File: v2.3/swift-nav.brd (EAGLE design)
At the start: 53 x 53 mm, 150 parts, among them J1 SMA_EDGE, J6 ZX62-B-5PA, Q1 IRLML6401, U1 6SLX9FTG256, U10 MAX2769, U12 PT7M8206B33TA5EX, U13 M25PX80, U2 LTC3407A_DFN, U3 STM32-M-64-LQFP, U4 7Q-16.368MBG-T, U5 SMA_PATCH_SMDGND, U6 93LC56BT-I/OT, U7 FT232HQ, U8 B4050, U9 XC2401, X3 FPGA DEBUG, X4 NX5032GA-12M, X5 CONN_5-2

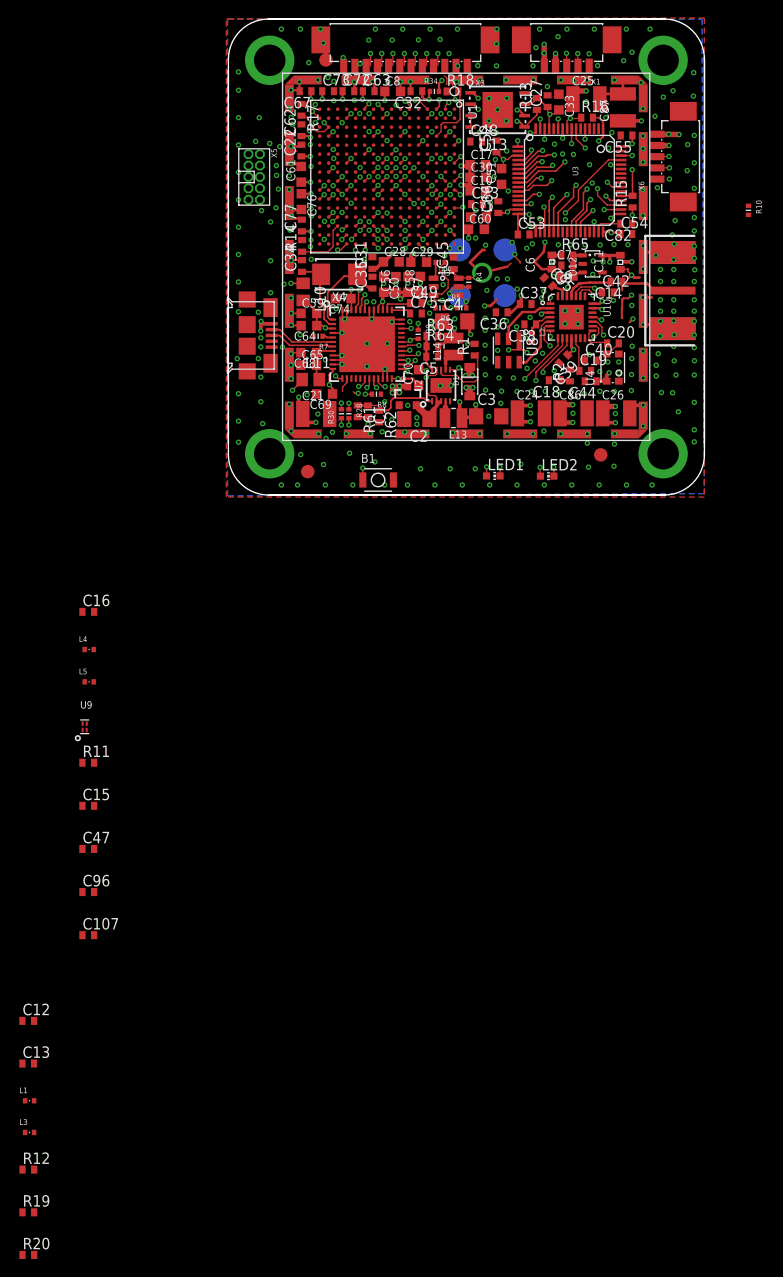
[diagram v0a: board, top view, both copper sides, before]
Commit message: Changed cap footprints to smaller versions
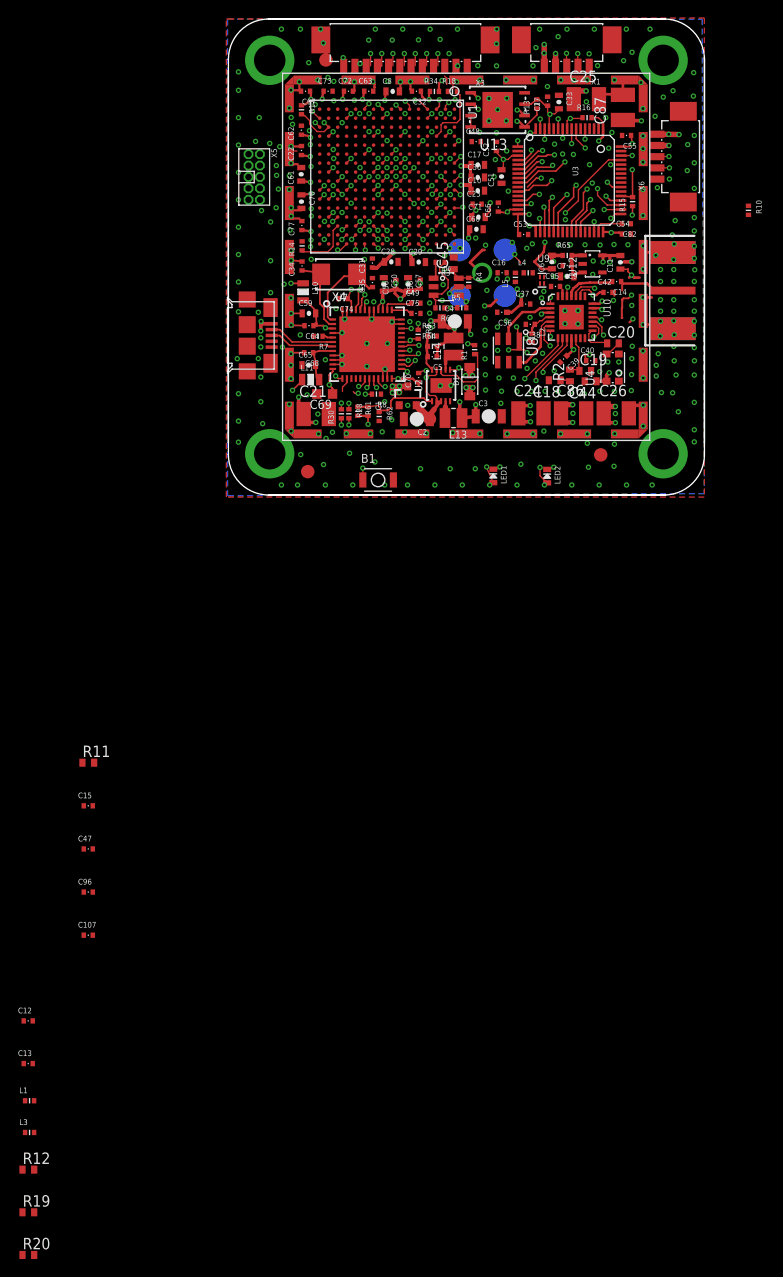
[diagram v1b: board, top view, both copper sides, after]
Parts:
- C1, C107, C12, C13, C14, C15, C16, C22, C23, C27, C31, C32, C34, C35, C36, C37, C38, C39, C40, C42, C47, C48, C49, C5, C52, C53, C54, C55, C62, C63, C66, C67, C72, C73, C75, C77, C82, C9, C95, C96: device rcl:C0402 -> pel_dipol_comp:0402-CAP
- C10, C17, C28, C29, C30, C33, C50, C51, C57, C59, C60, C61, C65, C71, C76, C8: device rcl:C0603K -> pel_dipol_comp:0603-CAP
- C11, C6, C7: device capsmd:0603 -> pel_dipol_comp:0603-CAP
- C2, C3, C4: device rcl:C1206 -> pel_dipol_comp:1206-CAP
- C21, C24, C25, C26, C86, C87: device rcl:C1210K -> rcl:C1210
- C56, C58, C64, C68, C70, C74: device rcl:C0603K -> pel_dipol_comp:0402-CAP
- L10, L11: device rcl:R0805 -> pel_dipol_comp:0805-IND
- L4: value 3.3nH -> 5.1nH
- L5: value 5.1nH -> 3.3nH
- LED1, LED2: device led:CHIP-LED0603 -> pel_dipol_comp:0603-LED
- R1, R13, R14, R15, R16, R17, R18, R61, R62, R63, R64, R65: device rcl:R0402 -> pel_dipol_comp:0402-RES
- moved U9 71.2 mm to (38.3, 27.3)
- moved L5 65.4 mm to (35.4, 27.6), turned to 90 degrees
- moved L4 64.4 mm to (36.8, 28.1)
- moved C16 59.6 mm to (33.9, 28.1)
- moved C95 0.95 mm to (39.8, 26.6), turned to 0 degrees
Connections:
- new net N$1: X3.12
- net FPGA_DONE: now also R16.P$1; no longer R16.1
- net FPGA_INIT_B: now also R17.P$2; no longer R17.2
- net FPGA_PROGRAM_B: now also R15.P$2; no longer R15.2
- net GND: now also C10.P$2, C107.P$2, C11.P$1, C12.P$1, C13.P$1, C15.P$1, C17.P$2, C2.P$2, C22.P$2, C23.P$2, C27.P$2, C28.P$2, C29.P$2, C3.P$2, C30.P$2, C31.P$2, C32.P$2, C33.P$1, C34.P$2, C35.P$2, C36.P$2, C37.P$2, C38.P$2, C39.P$2, C4.P$2, C40.P$2, C42.P$2, C47.P$1, C48.P$2, C49.P$2, C50.P$1, C51.P$1, C52.P$2, C53.P$2, C54.P$2, C55.P$2, C56.P$2, C57.P$1, C58.P$2, C59.P$1, C6.P$1, C60.P$2, C61.P$2, C62.P$2, C63.P$2, C64.P$2, C65.P$1, C66.P$2, C67.P$2, C68.P$2, C7.P$1, C70.P$2, C71.P$2, C72.P$2, C73.P$2, C74.P$2, C75.P$2, C76.P$2, C77.P$2, C8.P$2, C82.P$1, C9.P$2, C96.P$2, L5.P$1, R14.P$2, R18.P$1, R62.P$2, R63.P$2; no longer C10.2, C107.2, C11.1, C12.1, C13.1, C15.1, C17.2, C2.2, C22.2, C23.2, C27.2, C28.2, C29.2, C3.2, C30.2, C31.2, C32.2, C33.1, C34.2, C35.2, C36.2, C37.2, C38.2, C39.2, C4.2, C40.2, C42.2, C47.1, C48.2, C49.2, C50.1, C51.1, C52.2, C53.2, C54.2, C55.2, C56.2, C57.1, C58.2, C59.1, C6.1, C60.2, C61.2, C62.2, C63.2, C64.2, C65.1, C66.2, C67.2, C68.2, C7.1, C70.2, C71.2, C72.2, C73.2, C74.2, C75.2, C76.2, C77.2, C8.2, C82.1, C9.2, C96.2, L4.P$1, R14.2, R18.1, R62.2, R63.2
- net JTAG_RST: now also C32.P$1; no longer C32.1
- net N$11: now also C95.P$2; no longer C95.2
- net N$14: now also C16.P$1; no longer C16.1
- net N$15: now also C35.P$1; no longer C35.1
- net N$16: now also R1.P$1; no longer R1.1
- net N$19: now also C49.P$1; no longer C49.1
- net N$2: now also L4.P$2; no longer L5.P$1
- net N$21: now also C65.P$2, C68.P$1, L11.P$2; no longer C65.2, C68.1, L11.2
- net N$22: now also C38.P$1; no longer C38.1
- net N$29: now also C59.P$2, C64.P$1, L10.P$2; no longer C59.2, C64.1, L10.2
- net N$30: now also C14.P$2; no longer C14.2
- net N$31: now also R18.P$2; no longer R18.2
- net N$32: now also C75.P$1; no longer C75.1
- net N$34: now also R14.P$1; no longer R14.1
- net N$35: now also C16.P$2, L4.P$1; no longer C16.2, L4.P$2
- net N$36: now also C95.P$1; no longer C95.1
- net N$37: now also C12.P$2, C13.P$2; no longer C12.2, C13.2
- net N$41: now also C15.P$2, C47.P$2; no longer C15.2, C47.2
- net N$53: now also C1.P$1, R61.P$1, R62.P$1; no longer C1.1, R61.1, R62.1
- net N$54: now also C5.P$2, R63.P$1, R64.P$1; no longer C5.2, R63.1, R64.1
- net N$56: now also C7.P$2, C9.P$1, R65.P$2; no longer C7.2, C9.1, R65.2
- net N$8: now also C14.P$1; no longer C14.1
- net N$9: now also C34.P$1; no longer C34.1
- net SPI2NSS_FLASH: now also R13.P$1; no longer R13.1
- net V+: no longer X3.12
- net VCC: now also C11.P$2, C36.P$1, C37.P$1, C39.P$1, C40.P$1, C42.P$1; no longer C11.2, C36.1, C37.1, C39.1, C40.1, C42.1
- net VCCINT: now also C10.P$1, C17.P$1, C28.P$1, C29.P$1, C30.P$1, C31.P$1, C4.P$1, C5.P$1, R64.P$2; no longer C10.1, C17.1, C28.1, C29.1, C30.1, C31.1, C4.1, C5.1, R64.2
- net VCCIO: now also C1.P$2, C107.P$1, C22.P$1, C23.P$1, C27.P$1, C3.P$1, C33.P$2, C48.P$1, C50.P$2, C51.P$2, C52.P$1, C53.P$1, C54.P$1, C55.P$1, C56.P$1, C57.P$2, C58.P$1, C60.P$1, C61.P$1, C62.P$1, C63.P$1, C67.P$1, C70.P$1, C71.P$1, C72.P$1, C73.P$1, C74.P$1, C76.P$1, C77.P$1, C8.P$1, C96.P$1, L10.P$1, L11.P$1, R13.P$2, R15.P$1, R16.P$2, R17.P$1, R61.P$2; no longer C1.2, C107.1, C22.1, C23.1, C27.1, C3.1, C33.2, C48.1, C50.2, C51.2, C52.1, C53.1, C54.1, C55.1, C56.1, C57.2, C58.1, C60.1, C61.1, C62.1, C63.1, C67.1, C70.1, C71.1, C72.1, C73.1, C74.1, C76.1, C77.1, C8.1, C96.1, L10.1, L11.1, R13.2, R15.1, R16.2, R17.1, R61.2
- net VDD: now also C2.P$1, C6.P$2, R1.P$2, R65.P$1; no longer C2.1, C6.2, R1.2, R65.1
- net VSS1: now also C66.P$1; no longer C66.1
- net VSS2: now also C82.P$2; no longer C82.2
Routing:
- net N$14: track 3.46 -> 0.00 mm
- net VCCIO: track 143.7 -> 146.7 mm
- net GND: track 80.4 -> 81.9 mm
- net N$11: track 1.89 -> 0.70 mm
- net N$55: track 25.5 -> 26.5 mm
- net N$24: track 20.6 -> 21.5 mm
- net VCC: track 14.3 -> 15.0 mm
- net N$29: track 5.97 -> 6.50 mm
- net VCCINT: track 76.1 -> 76.7 mm

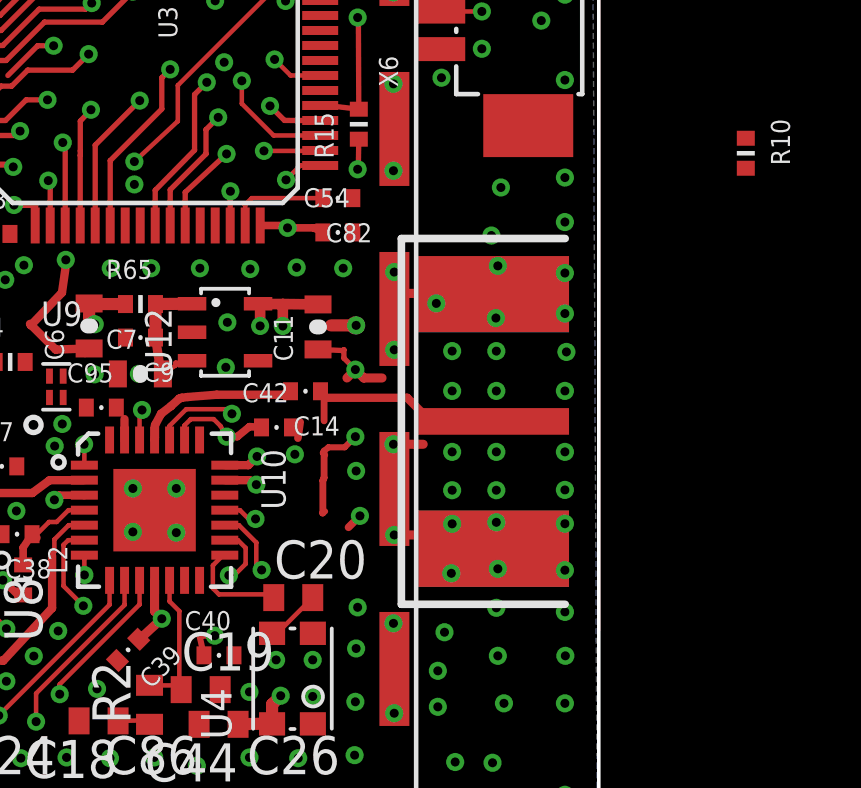
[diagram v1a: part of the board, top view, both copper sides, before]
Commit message: Moved LNA2 SMA to line up with shield opening better
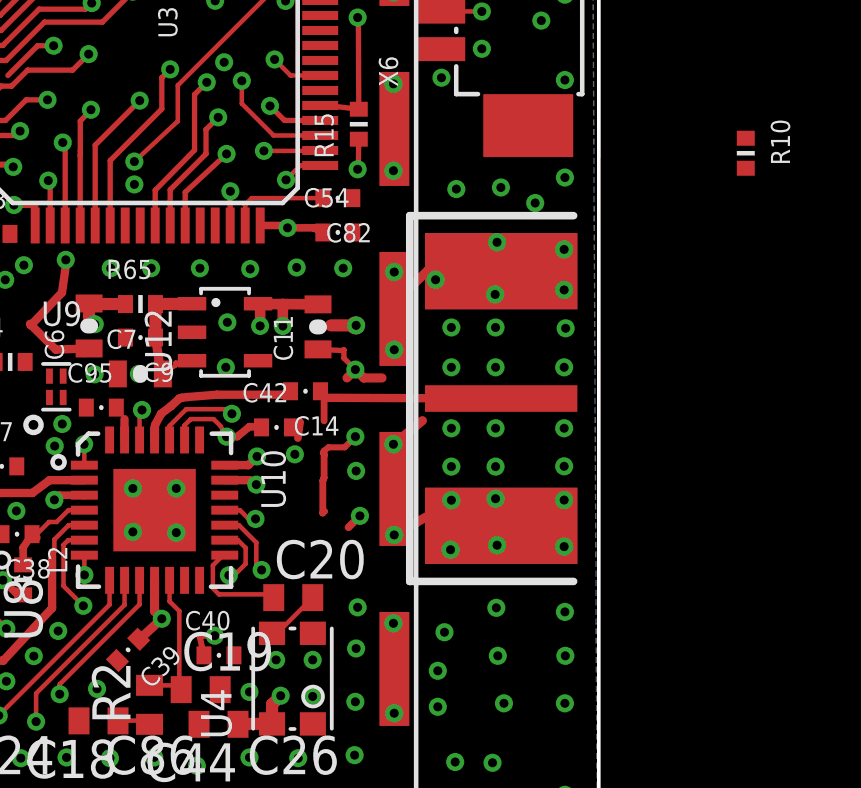
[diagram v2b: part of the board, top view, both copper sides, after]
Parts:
- moved J1 0.81 mm to (55.7, 26.9)
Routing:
- net GND: track 81.9 -> 82.6 mm
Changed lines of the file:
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@@
 <layer number="49" name="Reference" color="7" fill="1" visible="no" active="yes"/>
 <layer number="50" name="dxf" color="7" fill="1" visible="no" active="no"/>
-<layer number="51" name="tDocu" color="7" fill="1" visible="yes" active="yes"/>
+<layer number="51" name="tDocu" color="7" fill="1" visible="no" active="yes"/>
 <layer number="52" name="bDocu" color="7" fill="1" visible="no" active="yes"/>
 <layer number="53" name="tGND_GNDA" color="7" fill="9" visible="no" active="no"/>
@@
 <element name="B1" library="jobygnss" package="B3U-1000P" value="B3U-1000P" x="20.066" y="5.08"/>
 <element name="U5" library="joby_robotics" package="SMA_PATCH_SMDGND" value="SMA_PATCH_SMDGND" x="29.9" y="29.9" rot="MR270"/>
-<element name="J1" library="swift-nav" package="SMA_EDGE" value="SMA_EDGE" x="55.407559375" y="26.162" smashed="yes" rot="R270"/>
+<element name="J1" library="swift-nav" package="SMA_EDGE" value="SMA_EDGE" x="55.686959375" y="26.924" smashed="yes" rot="R270"/>
 <element name="C2" library="pel_dipol_comp" package="1206-CAP" value="10uF" x="24.3796" y="11.8646" rot="R180"/>
 <element name="C3" library="pel_dipol_comp" package="1206-CAP" value="10uF" x="32.385" y="12.1666"/>
@@
 <via x="55.2704" y="16.764" extent="1-16" drill="0.3"/>
 <via x="55.2704" y="19.812" extent="1-16" drill="0.3"/>
-<via x="55.2704" y="22.752" extent="1-16" drill="0.3"/>
-<via x="55.2704" y="25.146" extent="1-16" drill="0.3"/>
-<via x="55.2704" y="27.178" extent="1-16" drill="0.3"/>
-<via x="55.2704" y="31.107" extent="1-16" drill="0.3"/>
+<via x="55.245" y="23.5394" extent="1-16" drill="0.3"/>
+<via x="55.245" y="25.9334" extent="1-16" drill="0.3"/>
+<via x="55.245" y="27.9654" extent="1-16" drill="0.3"/>
+<via x="55.245" y="31.8944" extent="1-16" drill="0.3"/>
 <via x="55.2704" y="34.29" extent="1-16" drill="0.3"/>
 <via x="55.2704" y="37.5412" extent="1-16" drill="0.3"/>
@@
 <via x="25.4254" y="10.2616" extent="1-16" drill="0.3"/>
 <via x="10.1854" y="13.5128" extent="1-16" drill="0.3"/>
-<via x="52.9844" y="27.178" extent="1-16" drill="0.3"/>
-<via x="52.9844" y="25.146" extent="1-16" drill="0.3"/>
+<via x="52.959" y="27.9654" extent="1-16" drill="0.3"/>
+<via x="52.959" y="25.9334" extent="1-16" drill="0.3"/>
 <wire x1="31.9278" y1="30.6832" x2="31.6738" y2="30.6832" width="0.3048" layer="1"/>
 <wire x1="31.6738" y1="30.6832" x2="30.3022" y2="29.3116" width="0.3048" layer="1"/>
@@
 <wire x1="31.9278" y1="24.4602" x2="32.5882" y2="24.4602" width="0.3048" layer="1"/>
 <wire x1="32.5882" y1="24.4602" x2="33.274" y2="25.146" width="0.3048" layer="1"/>
-<wire x1="49.5808" y1="22.3774" x2="51.0032" y2="22.3774" width="0.3048" layer="1"/>
-<wire x1="51.0032" y1="22.3774" x2="51.054" y2="22.3266" width="0.3048" layer="1"/>
+<wire x1="49.5808" y1="22.3774" x2="50.9778" y2="23.1648" width="0.3048" layer="1"/>
+<wire x1="50.9778" y1="23.1648" x2="51.0286" y2="23.114" width="0.3048" layer="1"/>
 <wire x1="49.586" y1="29.91" x2="49.586" y2="30.1042" width="0.3048" layer="1"/>
 <wire x1="49.586" y1="30.1042" x2="49.911" y2="30.4292" width="0.3048" layer="1"/>
-<wire x1="49.911" y1="30.4292" x2="50.7492" y2="30.4292" width="0.3048" layer="1"/>
-<wire x1="50.7492" y1="30.4292" x2="50.7746" y2="30.4038" width="0.3048" layer="1"/>
-<via x="51.5112" y="27.178" extent="1-16" drill="0.3"/>
-<via x="51.5112" y="25.146" extent="1-16" drill="0.3"/>
+<wire x1="49.911" y1="30.4292" x2="50.7238" y2="31.2166" width="0.3048" layer="1"/>
+<wire x1="50.7238" y1="31.2166" x2="50.7492" y2="31.1912" width="0.3048" layer="1"/>
+<via x="51.4858" y="27.9654" extent="1-16" drill="0.3"/>
+<via x="51.4858" y="25.9334" extent="1-16" drill="0.3"/>
 <via x="8.1026" y="29.4894" extent="1-16" drill="0.3"/>
 <via x="8.1026" y="25.9334" extent="1-16" drill="0.3"/>
@@
 <via x="53.2384" y="16.764" extent="1-16" drill="0.3"/>
 <via x="51.2564" y="19.134" extent="1-16" drill="0.3"/>
-<via x="52.9844" y="22.798" extent="1-16" drill="0.3"/>
-<via x="51.5112" y="22.748" extent="1-16" drill="0.3"/>
-<via x="53.0344" y="31.346" extent="1-16" drill="0.3"/>
+<via x="52.959" y="23.5854" extent="1-16" drill="0.3"/>
+<via x="51.4858" y="23.5354" extent="1-16" drill="0.3"/>
+<via x="53.009" y="32.1334" extent="1-16" drill="0.3"/>
 <via x="49.5554" y="41.9608" extent="1-16" drill="0.3"/>
 <via x="6.8326" y="45.4152" extent="1-16" drill="0.3"/>
@@
 <wire x1="48.4378" y1="23.0124" x2="48.0568" y2="22.6314" width="0.254" layer="1"/>
 <wire x1="46.370240625" y1="25.60263125" x2="46.446440625" y2="26.13968125" width="0.254" layer="1"/>
-<wire x1="49.5554" y1="25.4" x2="50.546" y2="25.4" width="0.3048" layer="1"/>
+<wire x1="49.5554" y1="25.4" x2="50.5206" y2="26.1874" width="0.3048" layer="1"/>
 <wire x1="48.2854" y1="27.8892" x2="48.3362" y2="27.8384" width="0.3048" layer="1"/>
 <wire x1="48.3362" y1="27.8384" x2="48.5648" y2="27.6098" width="0.3048" layer="1"/>
@@
 <via x="8.7122" y="35.3822" extent="1-16" drill="0.3"/>
 <via x="6.4262" y="42.7736" extent="1-16" drill="0.3"/>
-<via x="52.9844" y="28.506" extent="1-16" drill="0.3"/>
-<via x="51.5112" y="28.506" extent="1-16" drill="0.3"/>
-<via x="52.9844" y="23.868" extent="1-16" drill="0.3"/>
-<via x="51.5112" y="23.868" extent="1-16" drill="0.3"/>
+<via x="52.959" y="29.2934" extent="1-16" drill="0.3"/>
+<via x="51.4858" y="29.2934" extent="1-16" drill="0.3"/>
+<via x="52.959" y="24.6554" extent="1-16" drill="0.3"/>
+<via x="51.4858" y="24.6554" extent="1-16" drill="0.3"/>
 <contactref element="H2" pad="B3,0"/>
 <contactref element="H4" pad="B3,0"/>
@@
 <via x="41.81034375" y="41.31880625" extent="1-16" drill="0.3"/>
 <via x="43.9118" y="38.1328" extent="1-16" drill="0.3"/>
-<via x="55.3204" y="28.478" extent="1-16" drill="0.3"/>
-<via x="55.2704" y="23.878" extent="1-16" drill="0.3"/>
+<via x="55.295" y="29.2654" extent="1-16" drill="0.3"/>
+<via x="55.245" y="24.6654" extent="1-16" drill="0.3"/>
 <via x="52.9844" y="19.948" extent="1-16" drill="0.3"/>
 <via x="53.0344" y="18.348" extent="1-16" drill="0.3"/>
@@
 <via x="51.0344" y="17.848" extent="1-16" drill="0.3"/>
 <via x="51.0344" y="16.648" extent="1-16" drill="0.3"/>
-<via x="55.2704" y="32.807" extent="1-16" drill="0.3"/>
-<via x="52.8204" y="32.357" extent="1-16" drill="0.3"/>
-<via x="50.9844" y="30.096" extent="1-16" drill="0.3"/>
-<via x="55.2704" y="29.757" extent="1-16" drill="0.3"/>
-<via x="52.9704" y="29.607" extent="1-16" drill="0.3"/>
-<via x="55.2704" y="21.202" extent="1-16" drill="0.3"/>
-<via x="53.0344" y="21.248" extent="1-16" drill="0.3"/>
-<via x="51.4844" y="21.098" extent="1-16" drill="0.3"/>
+<via x="54.2798" y="33.442" extent="1-16" drill="0.3"/>
+<via x="51.652" y="33.9064" extent="1-16" drill="0.3"/>
+<via x="50.959" y="30.8834" extent="1-16" drill="0.3"/>
+<via x="55.245" y="30.5444" extent="1-16" drill="0.3"/>
+<via x="52.945" y="30.3944" extent="1-16" drill="0.3"/>
+<via x="55.245" y="21.9894" extent="1-16" drill="0.3"/>
+<via x="53.009" y="22.0354" extent="1-16" drill="0.3"/>
+<via x="51.459" y="21.8854" extent="1-16" drill="0.3"/>
 <via x="12.5484" y="31.0508" extent="1-16" drill="0.3"/>
 <via x="15.1249" y="40.8719" extent="1-16" drill="0.3"/>
@@
 <wire x1="9.3026" y1="4.5212" x2="-12.7" y2="-31.2" width="0" layer="19" extent="1-1"/>
 <wire x1="41.5925" y1="23.2029" x2="41.592" y2="23.2024" width="0" layer="19" extent="1-1"/>
+<wire x1="28.4" y1="49.35" x2="28.4226" y2="49.6062" width="0" layer="19" extent="1-1"/>
 <wire x1="31.75" y1="28.2702" x2="31.6484" y2="27.9654" width="0" layer="19" extent="1-1"/>
 <wire x1="46.446440625" y1="26.13968125" x2="46.157396875" y2="25.96188125" width="0" layer="19" extent="1-1"/>
@@
 <contactref element="J1" pad="P1"/>
 <contactref element="C14" pad="P$1"/>
-<wire x1="52.867559375" y1="26.162" x2="50.8" y2="26.162" width="0.2794" layer="1"/>
-<wire x1="50.8" y1="26.162" x2="50.0126" y2="26.9494" width="0.2794" layer="1"/>
-<wire x1="50.0126" y1="26.9494" x2="47.332503125" y2="26.9494" width="0.2794" layer="1"/>
+<wire x1="53.146959375" y1="26.924" x2="47.332503125" y2="26.9494" width="0.2794" layer="1"/>
 <wire x1="47.122959375" y1="27.167675" x2="47.24345" y2="27.044784375" width="0.2286" layer="1"/>
 <wire x1="47.24345" y1="27.044784375" x2="47.24345" y2="26.17993125" width="0.2286" layer="1"/>
